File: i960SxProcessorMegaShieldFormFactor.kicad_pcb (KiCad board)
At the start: 4 copper layers, 101.6 x 53.3 mm, 44 parts, among them P1 Power, P2 Data Lines Lower, P3 Data Lines Upper, P4 Address Lines, P5 PWM, P6 Serializable Pins, P7 1284p Direct Connection, U1 74HC245, U2 74HC245, U3 80960Sx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

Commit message: Added documentation text
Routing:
- net +5V: track 212.3 -> 213.9 mm
- net /DT\~R: track 100.7 -> 100.8 mm, vias 3 -> 2
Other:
- board text added: "74AHC04 74HC04"
- board text added: "74AHC08 / 74HC08"
- board text added: "74AHC174 / 74HC174"
- board text added: "74AHC573 / 74HC573"
- board text added: "Resistor Map R1 - 910 Ohm R2 - 560 - 1k Ohm R3 - 10k R4 - 10k R5 - 10k R6 - 10k R7 - 10k"
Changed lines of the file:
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@@
   (general
     (thickness 1.6)
-    (drawings 10)
+    (drawings 17)
     (tracks 996)
     (zones 0)
@@
     )
   )
+  (gr_text "74AHC08 / 74HC08" (at 153.9494 89.8017 90) (layer F.SilkS)
+    (effects (font (size 0.8 0.8) (thickness 0.1)))
+  )
+  (gr_text "74AHC174 / 74HC174" (at 172.15104 88.53932 90) (layer F.SilkS)
+    (effects (font (size 0.8 0.8) (thickness 0.1)))
+  )
+  (gr_text "74AHC174 / 74HC174" (at 165.92296 73.75144) (layer F.SilkS)
+    (effects (font (size 0.8 0.8) (thickness 0.1)))
+  )
+  (gr_text "74AHC573 / 74HC573" (at 188.3029 84.3915 90) (layer F.SilkS)
+    (effects (font (size 0.8 0.8) (thickness 0.1)))
+  )
+  (gr_text "74AHC573 / 74HC573" (at 189.82182 103.14432 90) (layer F.SilkS)
+    (effects (font (size 0.8 0.8) (thickness 0.1)))
+  )
+  (gr_text "74AHC04\n74HC04" (at 164.08654 104.59212 90) (layer F.SilkS)
+    (effects (font (size 0.8 0.8) (thickness 0.1)))
+  )
+  (gr_text "Resistor Map\nR1 - 910 Ohm\nR2 - 560 - 1k Ohm\nR3 - 10k\nR4 - 10k\nR5 - 10k\nR6 - 10k\nR7 - 10k" (at 140.82014 96.91116) (layer B.SilkS)
+    (effects (font (size 0.8 0.8) (thickness 0.1)) (justify left mirror))
+  )
   (gr_text "+5V\nA1\nA3\nA5\nA7\nA9\nA11\nA13\nA15\nD1\nD3\nD5\nD7\nD9\nD11\nD13\nD15\nGND" (at 201.85126 92.456) (layer F.SilkS)
     (effects (font (size 1.6 0.7) (thickness 0.15)) (justify left))
@@
   (segment (start 154.9146 95.4913) (end 153.0477 97.3582) (width 0.25) (layer Front) (net 2))
   (segment (start 155.68812 95.4913) (end 154.9146 95.4913) (width 0.25) (layer Front) (net 2))
+  (segment (start 154.44216 109.3978) (end 154.40406 109.4359) (width 0.25) (layer Front) (net 2))
+  (segment (start 155.99428 109.3978) (end 154.44216 109.3978) (width 0.25) (layer Front) (net 2))
   (segment (start 186.14062 79.6798) (end 191.083948 79.6798) (width 0.25) (layer Front) (net 3))
   (segment (start 191.083948 79.6798) (end 197.357748 73.406) (width 0.25) (layer Front) (net 3))
@@
   (segment (start 183.086321 92.894099) (end 174.217279 92.894099) (width 0.25) (layer Front) (net 61))
   (segment (start 174.217279 92.894099) (end 173.81728 92.4941) (width 0.25) (layer Front) (net 61))
-  (via (at 180.62956 98.11766) (size 0.8) (drill 0.4) (layers Front Back) (net 62))
-  (segment (start 176.85078 94.33888) (end 176.85078 89.83726) (width 0.25) (layer Back) (net 62))
-  (segment (start 180.62956 98.11766) (end 176.85078 94.33888) (width 0.25) (layer Back) (net 62))
   (via (at 179.18938 89.90584) (size 0.8) (drill 0.4) (layers Front Back) (net 62) (status 40000))
   (segment (start 179.1208 89.83726) (end 179.18938 89.90584) (width 0.25) (layer Back) (net 62))
@@
   (segment (start 177.551049 69.47499) (end 150.48901 69.47499) (width 0.25) (layer In1.Cu) (net 62))
   (segment (start 150.48901 69.47499) (end 149.098 70.866) (width 0.25) (layer In1.Cu) (net 62))
-  (segment (start 180.196565 98.550655) (end 180.196565 99.831668) (width 0.25) (layer Front) (net 62))
-  (segment (start 180.62956 98.11766) (end 180.196565 98.550655) (width 0.25) (layer Front) (net 62))
-  (segment (start 180.196565 108.146355) (end 180.196565 99.831668) (width 0.25) (layer Back) (net 62))
-  (segment (start 178.09538 109.22254) (end 179.12038 109.22254) (width 0.25) (layer Back) (net 62))
-  (via (at 180.196565 99.831668) (size 0.8) (drill 0.4) (layers Front Back) (net 62))
-  (segment (start 179.12038 109.22254) (end 180.196565 108.146355) (width 0.25) (layer Back) (net 62))
+  (segment (start 179.18938 96.67748) (end 180.62956 98.11766) (width 0.25) (layer In1.Cu) (net 62))
+  (segment (start 179.18938 89.90584) (end 179.18938 96.67748) (width 0.25) (layer In1.Cu) (net 62))
+  (via (at 180.82006 109.22762) (size 0.8) (drill 0.4) (layers Front Back) (net 62))
+  (segment (start 180.62956 109.03712) (end 180.82006 109.22762) (width 0.25) (layer In1.Cu) (net 62))
+  (segment (start 180.62956 98.11766) (end 180.62956 109.03712) (width 0.25) (layer In1.Cu) (net 62))
+  (segment (start 178.10046 109.22762) (end 178.09538 109.22254) (width 0.25) (layer Back) (net 62))
+  (segment (start 180.82006 109.22762) (end 178.10046 109.22762) (width 0.25) (layer Back) (net 62))
   (segment (start 138.398601 80.659321) (end 137.3124 79.57312) (width 0.25) (layer Back) (net 63))
   (segment (start 138.398601 83.951219) (end 138.398601 80.659321) (width 0.25) (layer Back) (net 63))

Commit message: Text addons done
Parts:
- added G***: LOGO, labitat/labitat_kicad_footprints.pretty:cc-by-sa_badge_8mm, F.Cu at (107.7, 110.4)
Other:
- board text added: "74AHC174"
- board text added: "A16"
- board text added: "A23 A22 A21 A20 A19 A18 A17"
- board text added: "A31 A30 A29 A28 A27 A26 A25 A24"
- board text added: "DT\~R ~DEN W\~R"
- board text added: "FAIL GND N\C ~RDY ALE ~AS ~LOCK ~BLAST"
- board text added: "HOLD HLDA ~INT3 INT2 INT1"
- board text added: "i960Sx Parallel Interface Board Contains Aux Hardware (C) 2021 Joshua Scoggins REV 2"
- board text added: "~INT0 ~RESET960 CLKO ~BE0 ~BE1 BA1 BA2 BA3"
- board text removed: "i960Sx Parallel Interface Board (C) 2021 Joshua Scoggins REV 2"

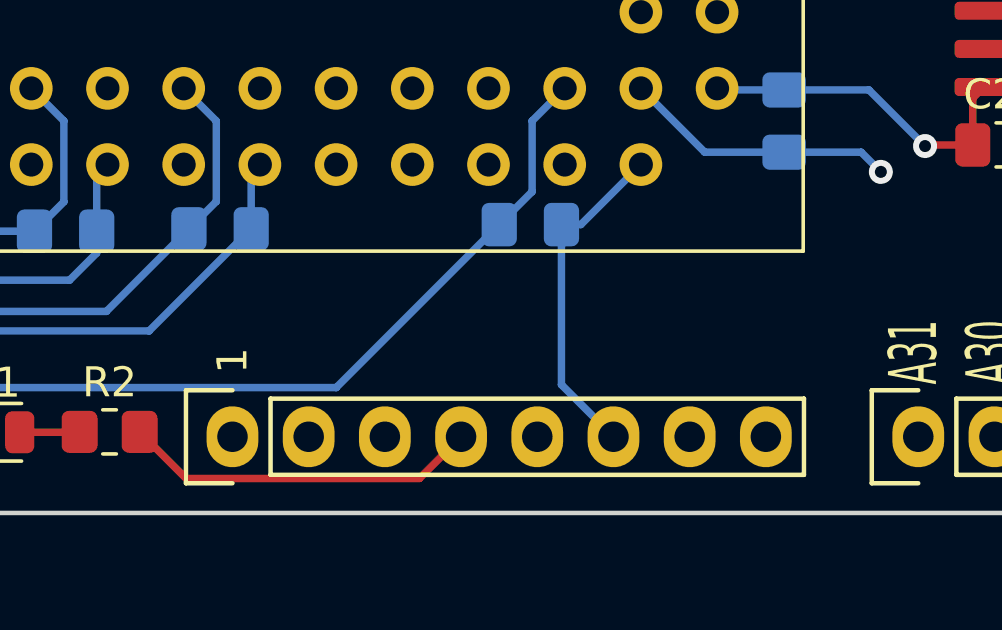
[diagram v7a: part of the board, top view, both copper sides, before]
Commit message: Add missing labelling
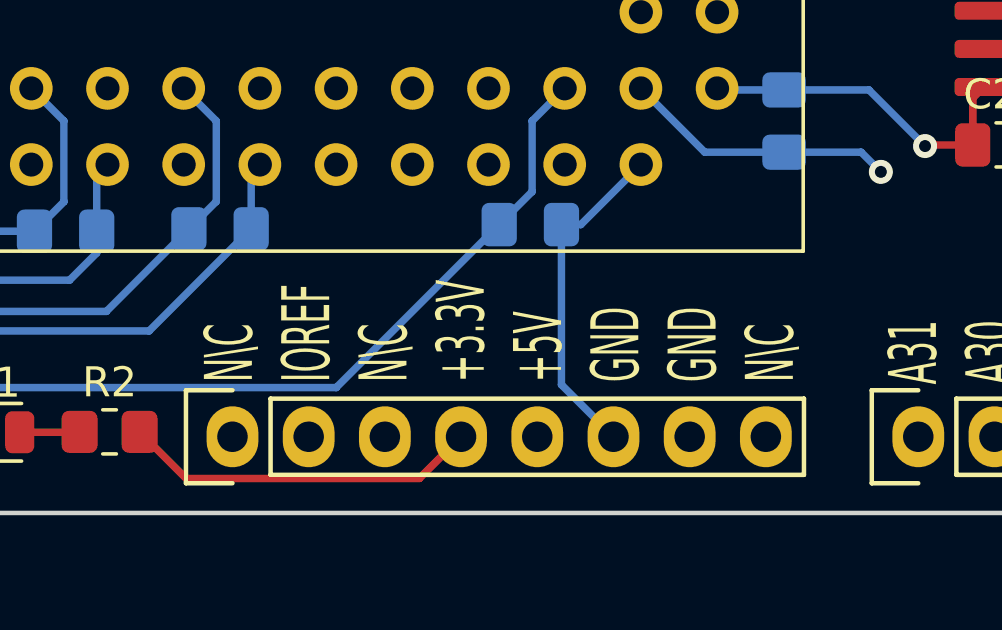
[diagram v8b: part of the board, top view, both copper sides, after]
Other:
- board text added: "N\C IOREF N\C +3.3V +5V GND GND N\C"
- board text removed: "1"
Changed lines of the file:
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@@
     (effects (font (size 0.8 0.8) (thickness 0.1)))
   )
-  (gr_text 1 (at 131.318 116.586 90) (layer F.SilkS)
-    (effects (font (size 1 1) (thickness 0.15)))
+  (gr_text "N\\C\nIOREF\nN\\C\n+3.3V\n+5V\nGND\nGND\nN\\C" (at 140.24102 117.30736 90) (layer F.SilkS)
+    (effects (font (size 1.6 0.8) (thickness 0.15)) (justify left))
   )
   (gr_line (start 202.438 120.396) (end 202.438 121.666) (angle 90) (layer Edge.Cuts) (width 0.15))
